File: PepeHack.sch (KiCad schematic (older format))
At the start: 23 parts, among them J1 SWD, J2 Bat, Q1 AO3407, Q2 AO3407, SW70 SW_Push, SW71 SW_DPDT_x2, U1 E73-2G4M08S1C-52840, U2 TP4054, U3 XC6220B331MR, Y1 32.768kHz

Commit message: Trackball sensor
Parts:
- added C1: 100nF, symbol Device:C_Small
- added C2: 4.7uF, symbol Device:C_Small
- added C? (x2): 1uF, symbol Device:C_Small
- added JP1: Jumper, symbol Jumper:SolderJumper_2_Open
- added R10: 39R, symbol Device:R_Small
- added R11: 10k, symbol Device:R_Small
- added U4: PMW3360DM-T2QU, symbol pmw3360dm-t2qu:PMW3360DM-T2QU
- added U5, U? (x4): SN74LVC1T45DCK, Package_TO_SOT_SMD:SOT-363_SC-70-6, symbol Logic_LevelTranslator:SN74LVC1T45DCK
- added U?: TLV70019, Package_TO_SOT_SMD:SOT-23-5, symbol Regulator_Linear:TLV70019_SOT23-5
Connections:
- net GND: now also C1.2, C2.2, C?.2, C?.2, U4.8 (GND), U5.2 (GND), U?.2 (GND), U?.2 (GND), U?.2 (GND), U?.2 (GND), U?.2 (GND), U?.5 (DIR)
- net VBAT: now also C?.1, U5.1 (VCCA), U5.5 (DIR), U?.1 (IN), U?.1 (VCCA), U?.1 (VCCA), U?.1 (VCCA), U?.1 (VCCA), U?.3 (EN), U?.5 (DIR), U?.5 (DIR)
- new net: R10.2, U4.15 (LED_P)
- new net: C1.1, C2.1, U4.3 (VDDPIX)
- new net: JP1.2 (B), R11.2
- new net MISO: JP1.1 (A), U4.12 (MISO)
- new net MOSI: U4.11 (MOSI), U?.4 (B)
- new net MOTION: U4.9 (MOTION), U?.4 (B)
- new net MOTION-H: U?.3 (A)
- new net MSIO: U?.4 (B)
- new net MSIO-H: U?.3 (A), U?.3 (A)
- new net NRESET: U4.7 (NRESET)
- new net SCLK: U4.10 (SCLK), U?.4 (B)
- new net SCLK-H: U?.3 (A)
- new net SS: U4.13 (NCS), U5.4 (B)
- new net SS-H: U5.3 (A), U?.5 (DIR)
- new net SVDD: C?.1, R10.1, R11.1, U4.4 (VDD), U4.5 (VDDIO), U5.6 (VCCB), U?.5 (OUT), U?.6 (VCCB), U?.6 (VCCB), U?.6 (VCCB), U?.6 (VCCB)
- no-connect marks 3 -> 8
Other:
- moved on the sheet: D70, D71, D72, J1, J2, Q1, Q2, R1, R2, R3, R4, R5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

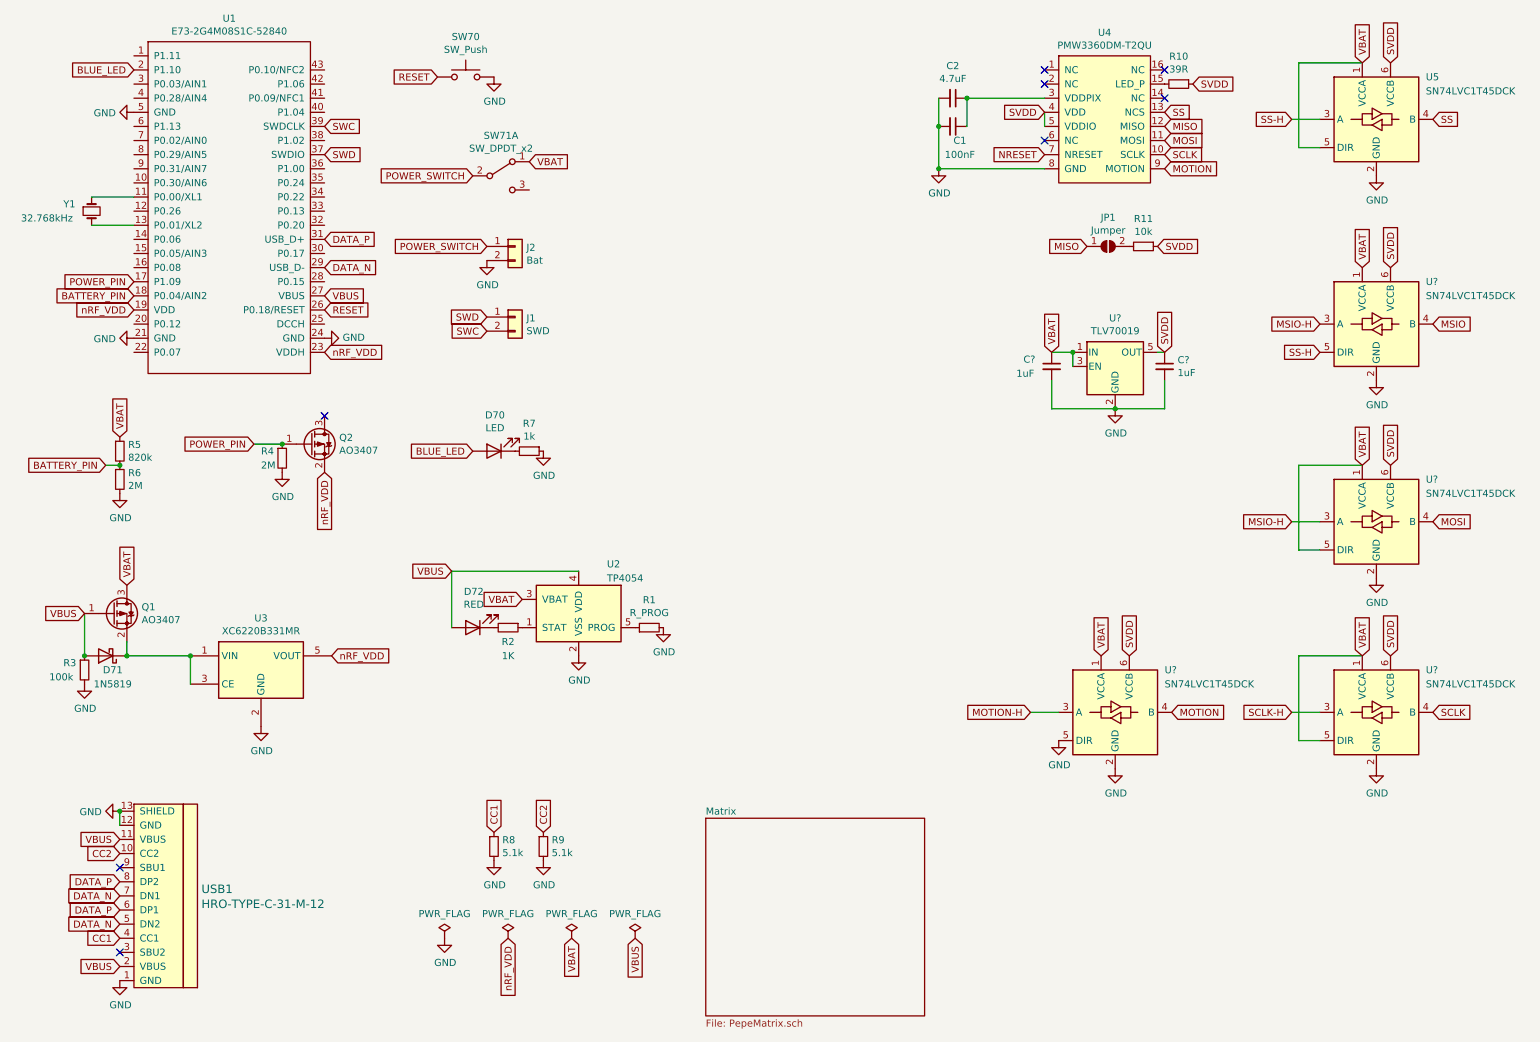
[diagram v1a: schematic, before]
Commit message: Simple keyboard matrix. Trackball sensor pcb + gerbers
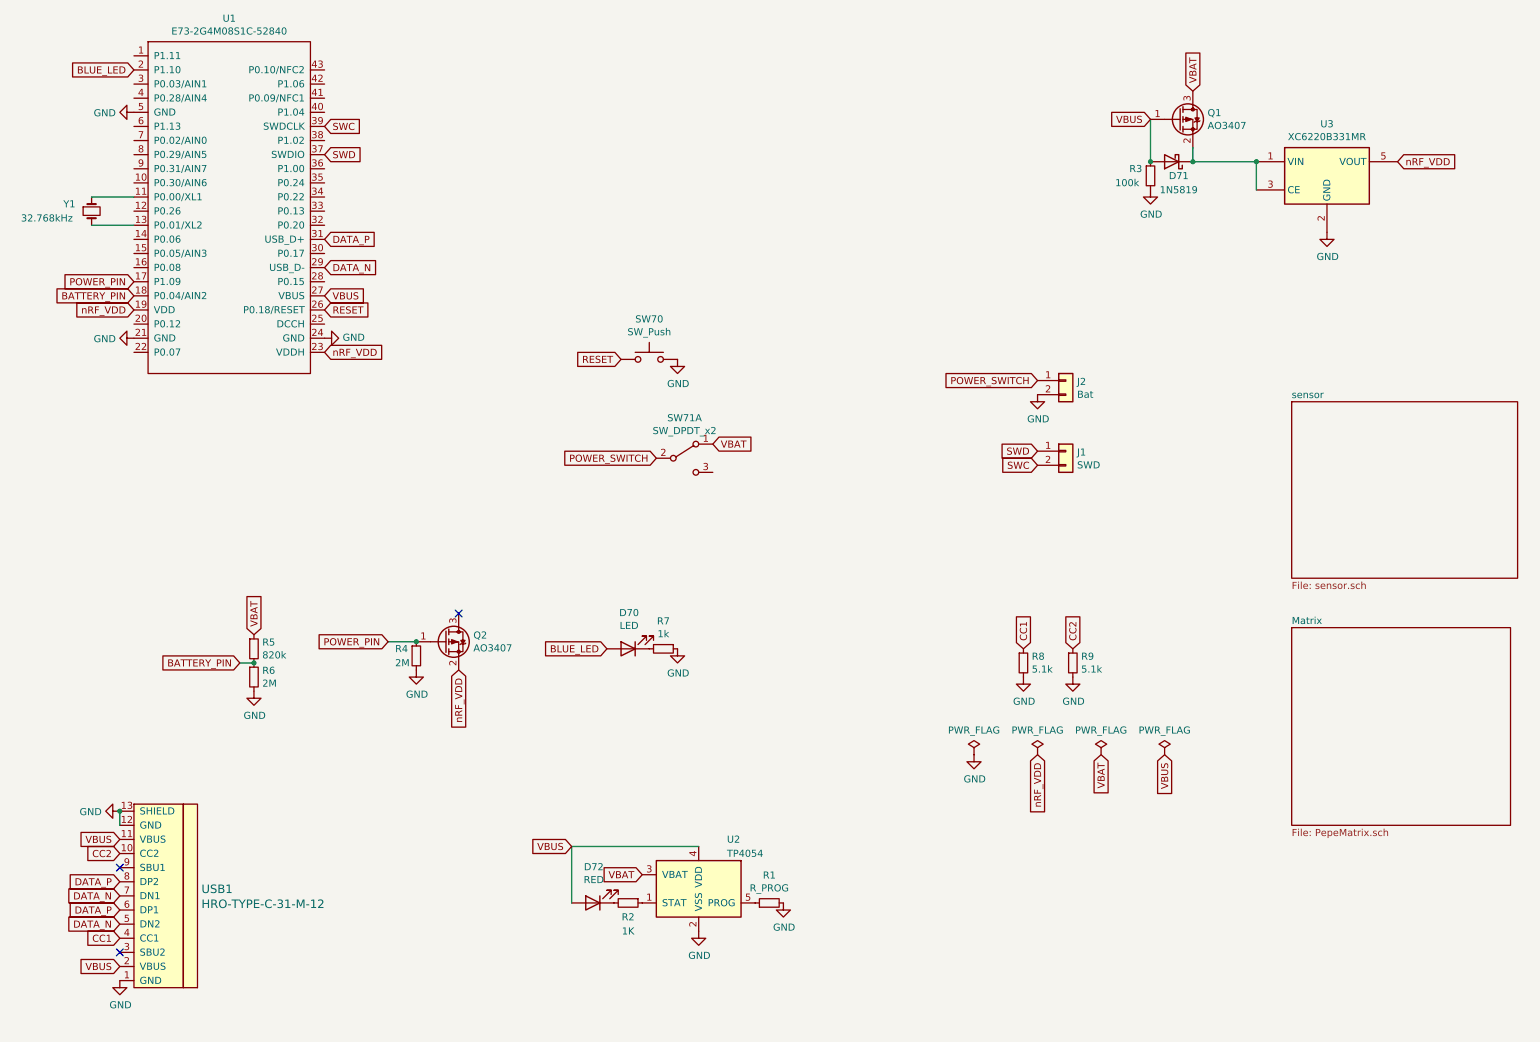
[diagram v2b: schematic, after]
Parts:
- removed C1: 100nF, symbol Device:C_Small
- removed C2: 4.7uF, symbol Device:C_Small
- removed C? (x2): 1uF, symbol Device:C_Small
- removed JP1: Jumper, symbol Jumper:SolderJumper_2_Open
- removed R10: 39R, symbol Device:R_Small
- removed R11: 10k, symbol Device:R_Small
- removed U4: PMW3360DM-T2QU, symbol pmw3360dm-t2qu:PMW3360DM-T2QU
- removed U5, U? (x4): SN74LVC1T45DCK, Package_TO_SOT_SMD:SOT-363_SC-70-6, symbol Logic_LevelTranslator:SN74LVC1T45DCK
- removed U?: TLV70019, Package_TO_SOT_SMD:SOT-23-5, symbol Regulator_Linear:TLV70019_SOT23-5
- D70, D72: footprint (none) -> LED_SMD:LED_0805_2012Metric_Pad1.15x1.40mm_HandSolder
- J1: footprint (none) -> Connector_PinHeader_2.54mm:PinHeader_1x02_P2.54mm_Vertical
- J2: footprint (none) -> Connector_JST:JST_PH_B2B-PH-K_1x02_P2.00mm_Vertical
- R1, R2, R3, R4, R5, R6, R7, R8, R9: footprint (none) -> Resistor_SMD:R_0805_2012Metric_Pad1.20x1.40mm_HandSolder
- SW70: footprint (none) -> bankkis_lib:tact_switch_1r
- SW71: footprint (none) -> Button_Switch_THT:SW_E-Switch_EG2219_DPDT_Angled
- U1: footprint (none) -> bankkis_lib:E73-2G4M08S1C-52840
- USB1: footprint (none) -> bankkis_lib:HRO-TYPE-C-31-M-12-HandSoldering
- Y1: footprint (none) -> Crystal:Crystal_SMD_0603-2Pin_6.0x3.5mm_HandSoldering
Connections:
- no-connect marks 8 -> 3
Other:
- moved on the sheet: D70, D71, D72, J1, J2, Q1, Q2, R1, R2, R3, R4, R5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
